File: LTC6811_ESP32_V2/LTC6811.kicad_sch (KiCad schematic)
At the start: 58 parts, among them J16 B7B-XH-A, J17 B7B-XH-A, Q40 NSV1C201MZ4, U14 LTC6811HG-1

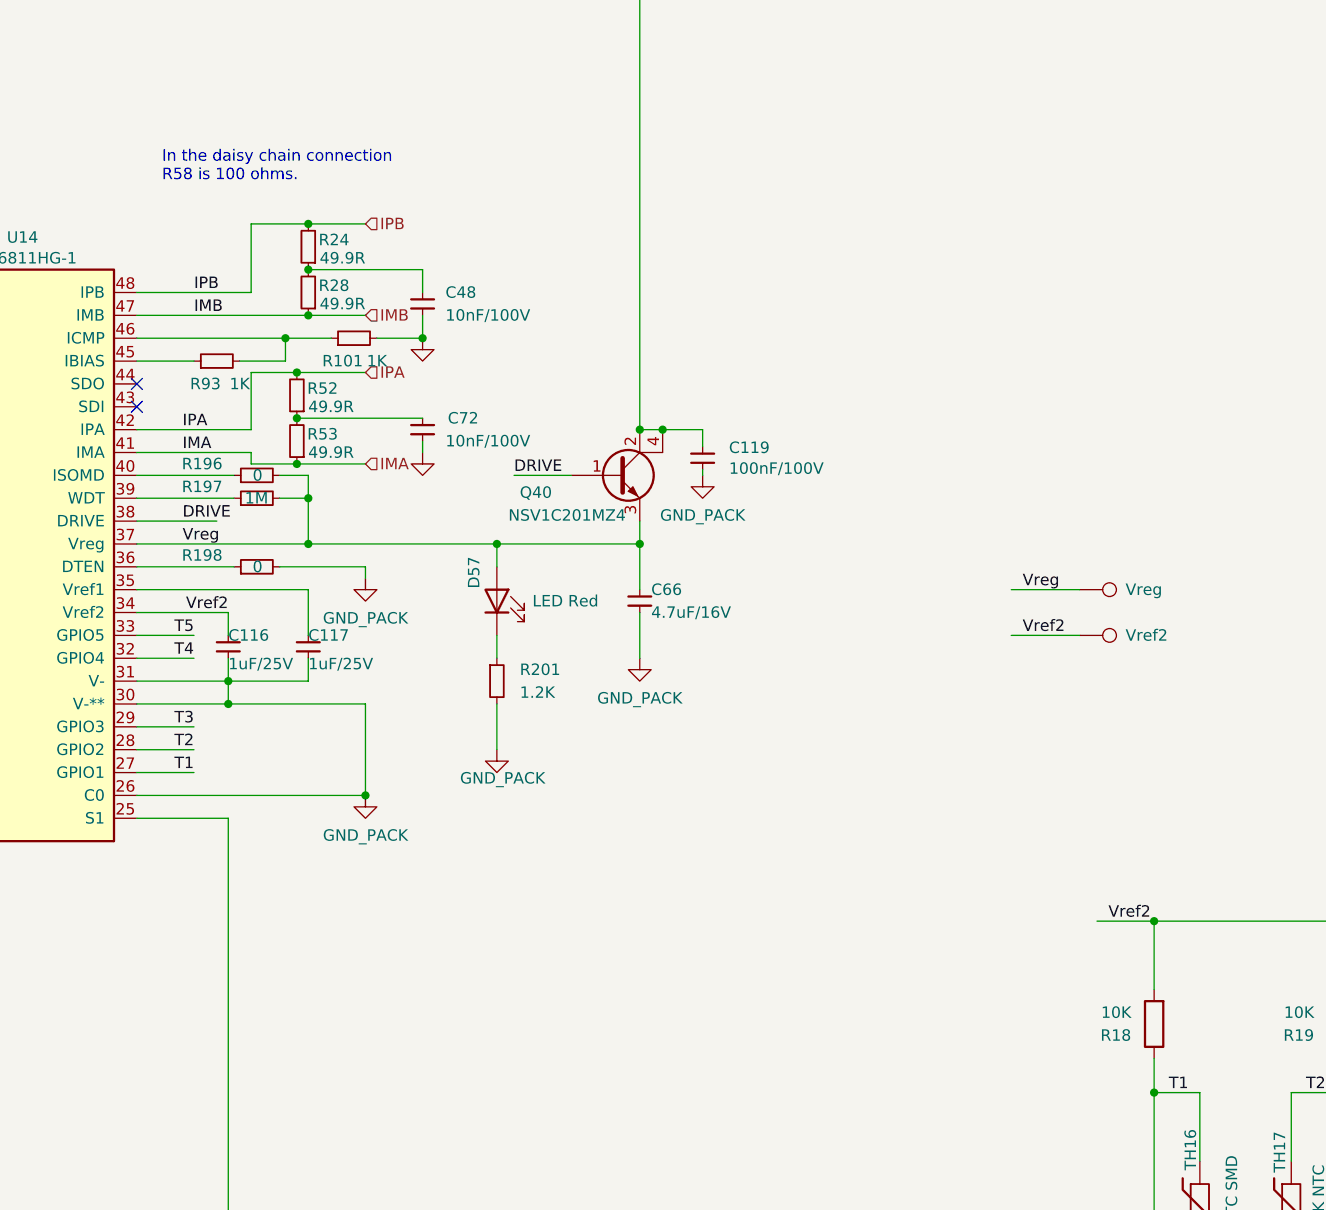
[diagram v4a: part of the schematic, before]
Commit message: Add 8P DIP switch and mcp23s17
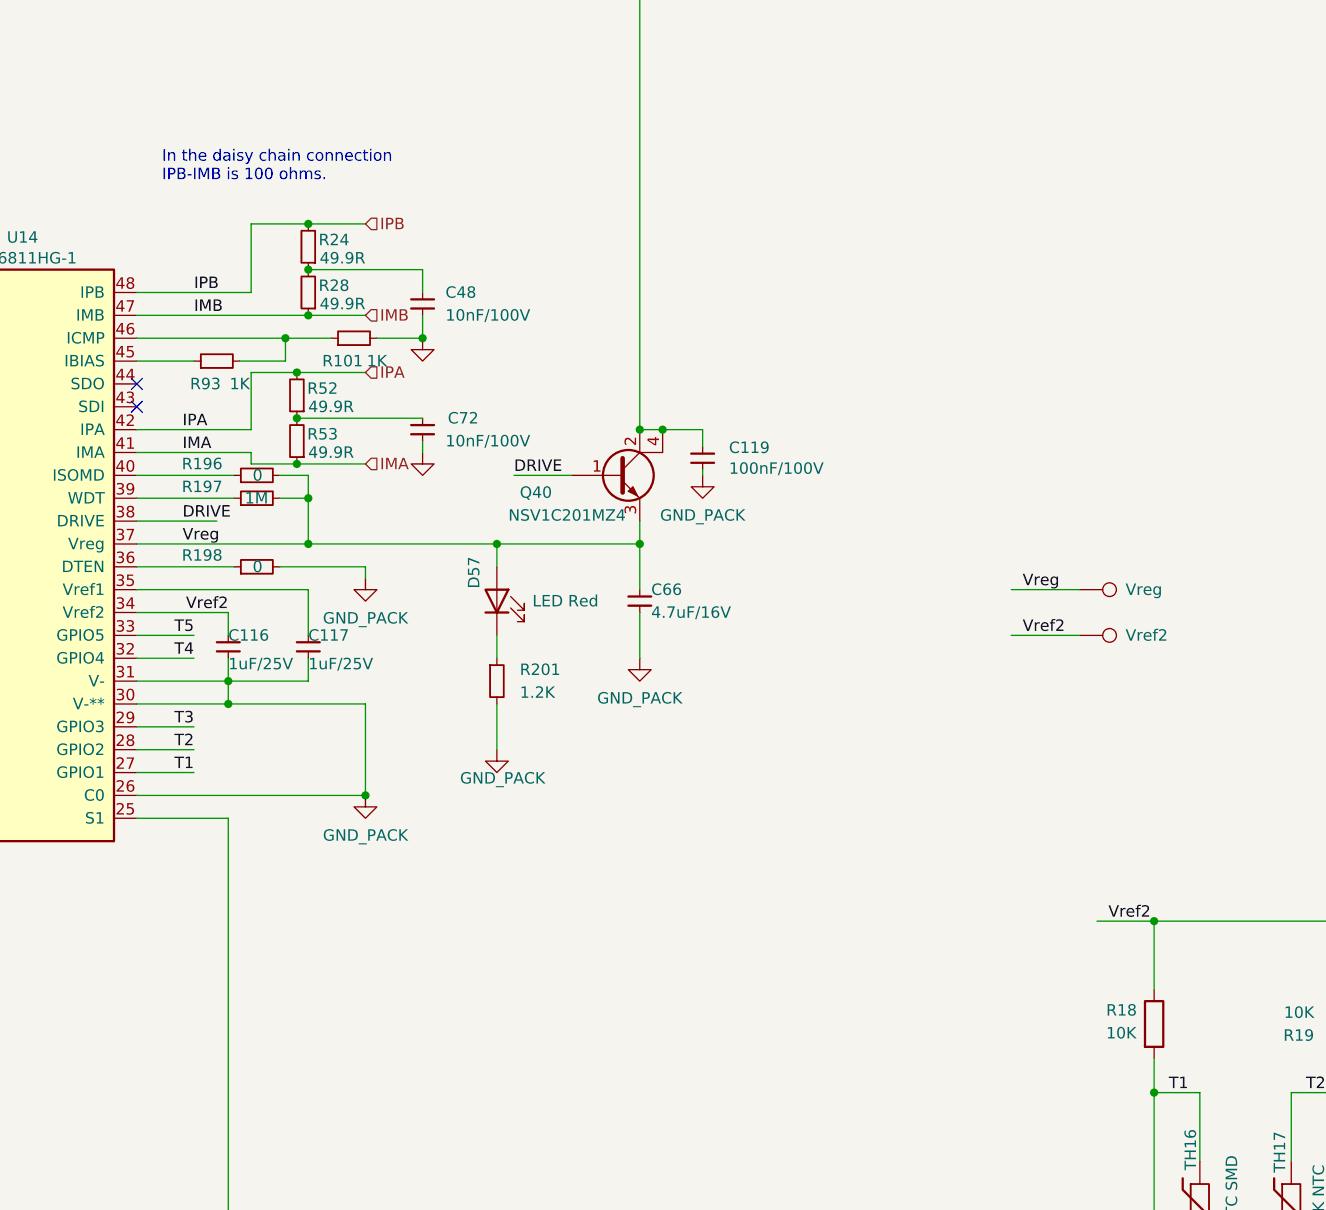
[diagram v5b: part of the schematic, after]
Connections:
- net T1: now also R18.2; no longer R18.1
- net Vref2: now also R18.1; no longer R18.2
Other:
- note added: "In the daisy chain connection IPB-IMB is 100 ohms."
- note removed: "In the daisy chain connection R58 is 100 ohms."
- moved on the sheet: R18
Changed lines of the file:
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@@
 		)
 	)
-	(text "In the daisy chain connection\nR58 is 100 ohms."
+	(text "In the daisy chain connection\nIPB-IMB is 100 ohms."
 		(exclude_from_sim no)
 		(at 212.344 102.108 0)
@@
 	(symbol
 		(lib_id "Library:R")
-		(at 322.58 195.58 180)
+		(at 322.58 195.58 0)
 		(unit 1)
 		(exclude_from_sim no)
@@
 		(dnp no)
 		(property "Reference" "R18"
-			(at 320.04 196.85 0)
+			(at 317.246 194.056 0)
 			(effects
 				(font
@@
 		)
 		(property "Value" "10K"
-			(at 320.04 194.31 0)
+			(at 317.246 196.596 0)
 			(effects
 				(font
@@
 		)
 		(property "Footprint" "Resistor_SMD:R_0603_1608Metric"
-			(at 324.358 195.58 90)
-			(effects
-				(font
+			(at 320.802 195.58 90)
+			(effects
+				(font
